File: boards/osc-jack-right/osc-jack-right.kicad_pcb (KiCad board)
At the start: 6 copper layers, 136.5 x 144 mm, 1068 parts, among them J1101 WQP518MA, J1102 WQP518MA, J1103 WQP518MA, J1104 WQP518MA, J1105 WQP518MA, J1106 WQP518MA, J1107 WQP518MA, J1108 WQP518MA, J1109 WQP518MA, J1110 WQP518MA, J1201 WQP518MA, J1202 WQP518MA, J1203 WQP518MA, J1204 WQP518MA, J1205 WQP518MA, J1206 WQP518MA, J1207 WQP518MA, J1208 WQP518MA, J1209 WQP518MA, J1210 WQP518MA, J1301 WQP518MA, J1302 WQP518MA, J1303 WQP518MA, J1304 WQP518MA, J1305 WQP518MA, J1306 WQP518MA, J1307 WQP518MA, J1308 WQP518MA, J1309 WQP518MA, J1310 WQP518MA, J1401 WQP518MA, J1402 WQP518MA, J1403 WQP518MA, J1404 WQP518MA, J1405 WQP518MA, J1406 WQP518MA, J1407 WQP518MA, J1408 WQP518MA, J1409 WQP518MA, J1410 WQP518MA, J1501 WQP518MA, J1502 WQP518MA, J1503 WQP518MA, J1504 WQP518MA, J1505 WQP518MA, J1506 WQP518MA, J1507 WQP518MA, J1508 WQP518MA, J1509 WQP518MA, J1510 WQP518MA, J1601 WQP518MA, J1602 WQP518MA, J1603 WQP518MA, J1604 WQP518MA, J1605 WQP518MA, J1606 WQP518MA, J1607 WQP518MA, J1608 WQP518MA, J1609 WQP518MA, J1610 WQP518MA, J1701 WQP518MA, J1702 WQP518MA, J1703 WQP518MA, J1704 WQP518MA, J1705 WQP518MA, J1706 WQP518MA, J1707 WQP518MA, J1708 WQP518MA, J1709 WQP518MA, J1710 WQP518MA, J1801 WQP518MA, J1802 WQP518MA, J1803 WQP518MA, J1804 WQP518MA, J1805 WQP518MA, J1806 WQP518MA, J1807 WQP518MA, J1808 WQP518MA, J1809 WQP518MA, J1810 WQP518MA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

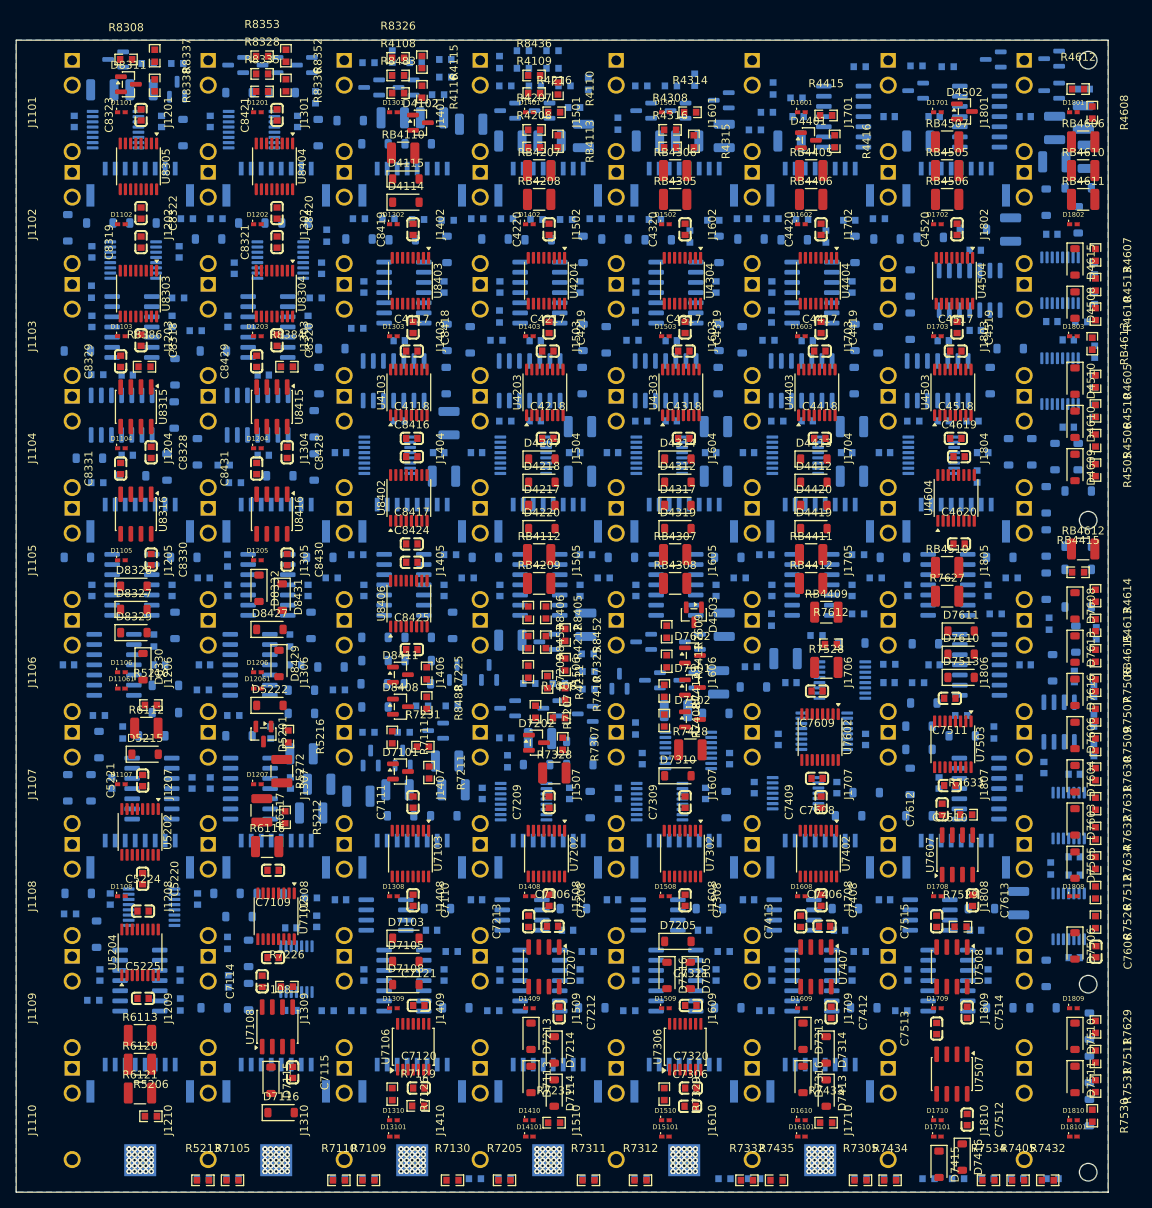
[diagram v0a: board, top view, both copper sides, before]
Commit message: Route osc-jack-right on CI: stage rail-fanout, open edges 1784 -> 1388
Adopted grid-routing stage pushed as soon as it was promoted.
Unvalidated draft; electrical and physical qualification NOT RUN.

Run: https://github.com/Takazudo/zudo-osc-hole-field/actions/runs/37351839697
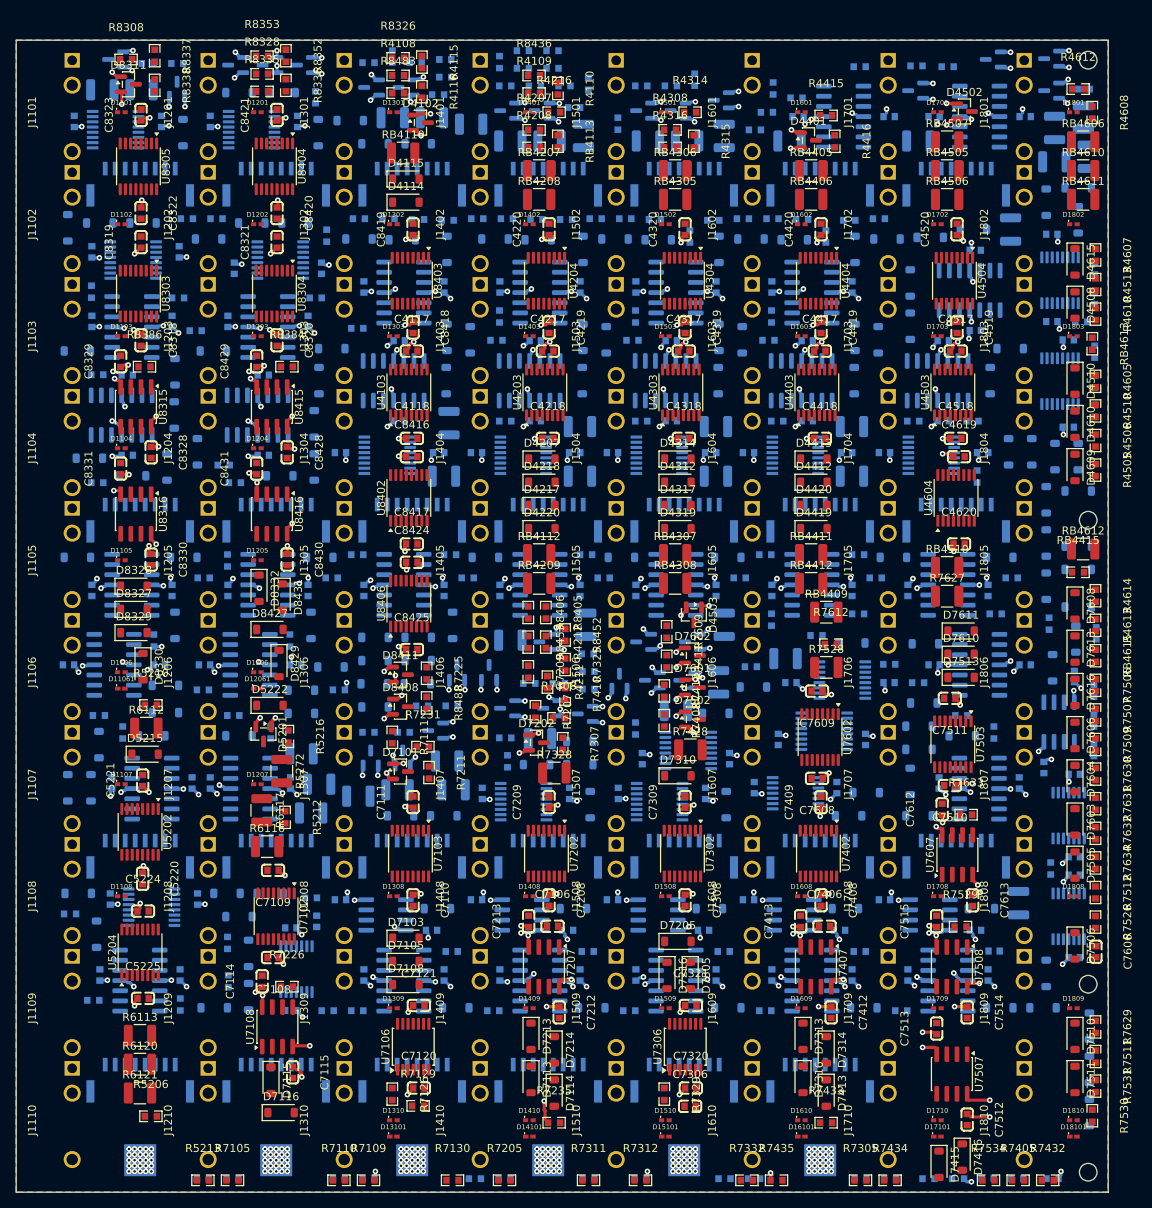
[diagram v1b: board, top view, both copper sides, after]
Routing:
- net +12V: track 0.00 -> 128.8 mm, vias 25 -> 227
- net -12V: track 0.00 -> 116.6 mm, vias 25 -> 219
